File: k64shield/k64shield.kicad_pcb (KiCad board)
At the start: 2 copper layers, 7 parts, among them J1 top_left_header_02x08, J2 bottom_left_header_02x06, J3 rpi_motor_driver_header, J4 top_right_header_02x10, J5 bottom_right_header_02x08, J6 camera_header_01x05, J7 servo_header_01x03

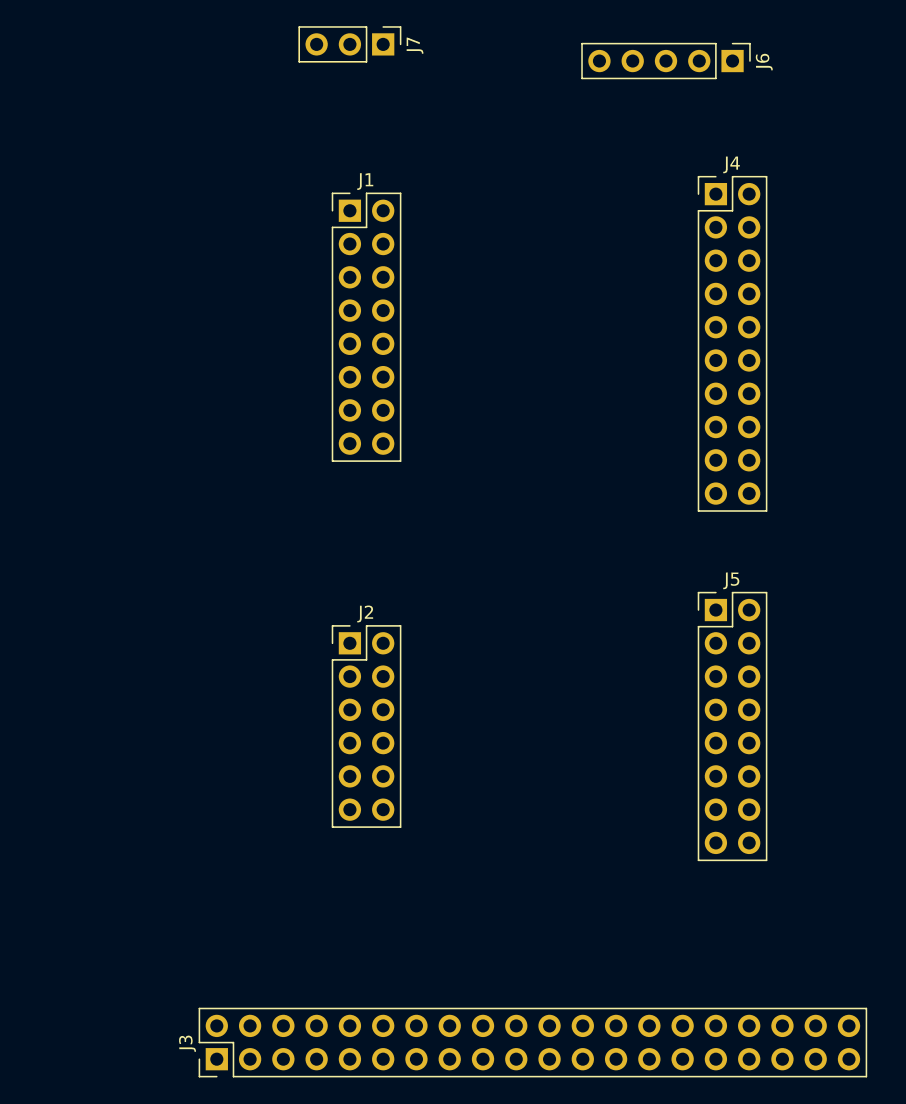
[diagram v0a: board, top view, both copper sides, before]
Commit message: Saving so I have a point to revert to - pins are very messed up
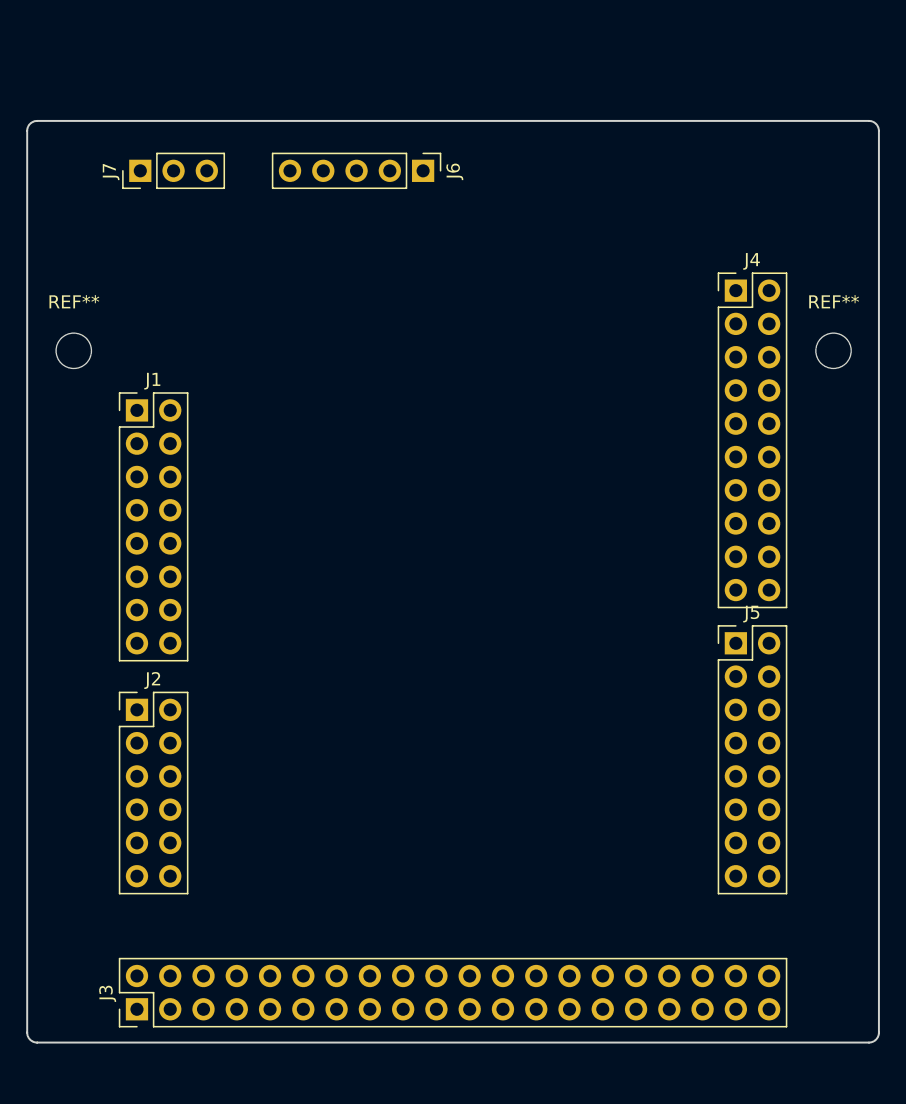
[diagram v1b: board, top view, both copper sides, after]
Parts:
- added REF**: MountingHole_2.7mm_M2.5, Mounting_Holes:MountingHole_2.7mm_M2.5, F.Cu at (149.9, 71.7)
- added REF**: MountingHole_2.7mm_M2.5, Mounting_Holes:MountingHole_2.7mm_M2.5, F.Cu at (91.9, 71.7)
- moved J6 25.1 mm to (118.6, 57.9)
- moved J1 22.3 mm to (96.8, 76.2)
- moved J7 20.9 mm to (97.0, 57.9), turned to 90 degrees
- moved J2 17.0 mm to (96.8, 99.1)
- moved J4 7.52 mm to (142.5, 67.1)
- moved J3 7.19 mm to (96.8, 121.9)
- moved J5 2.96 mm to (142.5, 94.0)
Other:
- board outline added: 65 x 70.4 mm
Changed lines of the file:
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@@
     (links 25)
     (no_connects 25)
-    (area 0 0 0 0)
+    (area 81.676572 49.378665 160.219429 129.802382)
     (thickness 1.6)
-    (drawings 0)
+    (drawings 8)
     (tracks 0)
     (zones 0)
-    (modules 7)
+    (modules 9)
     (nets 88)
   )
@@
     (pad_to_mask_clearance 0.2)
     (aux_axis_origin 0 0)
-    (visible_elements FFFFFF7F)
+    (grid_origin 79.248 130.556)
+    (visible_elements 7FFFFFFF)
     (pcbplotparams
       (layerselection 0x00030_80000001)
@@
     (add_net "Net-(J5-Pad9)")
   )
-  (module Pin_Headers:Pin_Header_Straight_2x08_Pitch2.54mm (layer F.Cu)
-    (at 113.03 60.96)
+  (module Mounting_Holes:MountingHole_2.7mm_M2.5 (layer F.Cu)
+    (at 149.948 71.65)
+    (descr "Mounting Hole 2.7mm, no annular, M2.5")
+    (tags "mounting hole 2.7mm no annular m2.5")
+    (attr virtual)
+    (fp_text reference REF** (at 0 -3.7) (layer F.SilkS)
+      (effects (font (size 1 1) (thickness 0.15)))
+    )
+    (fp_text value MountingHole_2.7mm_M2.5 (at 0 3.7) (layer F.Fab)
+      (effects (font (size 1 1) (thickness 0.15)))
+    )
+    (fp_text user %R (at 0.3 0) (layer F.Fab)
+      (effects (font (size 1 1) (thickness 0.15)))
+    )
+    (fp_circle (center 0 0) (end 2.7 0) (layer Cmts.User) (width 0.15))
+    (fp_circle (center 0 0) (end 2.95 0) (layer F.CrtYd) (width 0.05))
+    (pad 1 np_thru_hole circle (at 0 0) (size 2.7 2.7) (drill 2.7) (layers *.Cu *.Mask))
+  )
+  (module Pin_Headers:Pin_Header_Straight_2x08_Pitch2.54mm locked (layer F.Cu)
+    (at 96.774 76.2)
     (descr "Through hole straight pin header, 2x08, 2.54mm pitch, double rows")
     (tags "Through hole pin header THT 2x08 2.54mm double row")
@@
     )
   )
-  (module Pin_Headers:Pin_Header_Straight_2x06_Pitch2.54mm (layer F.Cu)
-    (at 113.03 93.98)
+  (module Pin_Headers:Pin_Header_Straight_2x06_Pitch2.54mm locked (layer F.Cu)
+    (at 96.774 99.06)
     (descr "Through hole straight pin header, 2x06, 2.54mm pitch, double rows")
     (tags "Through hole pin header THT 2x06 2.54mm double row")
@@
   )
   (module Pin_Headers:Pin_Header_Straight_2x20_Pitch2.54mm (layer F.Cu)
-    (at 102.87 125.73 90)
+    (at 96.774 121.92 90)
     (descr "Through hole straight pin header, 2x20, 2.54mm pitch, double rows")
     (tags "Through hole pin header THT 2x20 2.54mm double row")
@@
     )
   )
-  (module Pin_Headers:Pin_Header_Straight_2x10_Pitch2.54mm (layer F.Cu)
-    (at 140.97 59.69)
+  (module Pin_Headers:Pin_Header_Straight_2x10_Pitch2.54mm locked (layer F.Cu)
+    (at 142.494 67.056)
     (descr "Through hole straight pin header, 2x10, 2.54mm pitch, double rows")
     (tags "Through hole pin header THT 2x10 2.54mm double row")
@@
     )
   )
-  (module Pin_Headers:Pin_Header_Straight_2x08_Pitch2.54mm (layer F.Cu)
-    (at 140.97 91.44)
+  (module Pin_Headers:Pin_Header_Straight_2x08_Pitch2.54mm locked (layer F.Cu)
+    (at 142.494 93.98)
     (descr "Through hole straight pin header, 2x08, 2.54mm pitch, double rows")
     (tags "Through hole pin header THT 2x08 2.54mm double row")
@@
   )
   (module Pin_Headers:Pin_Header_Straight_1x05_Pitch2.54mm (layer F.Cu)
-    (at 142.24 49.53 270)
+    (at 118.618 57.912 270)
     (descr "Through hole straight pin header, 1x05, 2.54mm pitch, single row")
     (tags "Through hole pin header THT 1x05 2.54mm single row")
@@
   )
   (module Pin_Headers:Pin_Header_Straight_1x03_Pitch2.54mm (layer F.Cu)
-    (at 115.57 48.26 270)
+    (at 97.028 57.912 90)
     (descr "Through hole straight pin header, 1x03, 2.54mm pitch, single row")
     (tags "Through hole pin header THT 1x03 2.54mm single row")
-    (fp_text reference J7 (at 0 -2.33 270) (layer F.SilkS)
-      (effects (font (size 1 1) (thickness 0.15)))
-    )
-    (fp_text value servo_header_01x03 (at 0 7.41 270) (layer F.Fab)
+    (fp_text reference J7 (at 0 -2.33 90) (layer F.SilkS)
+      (effects (font (size 1 1) (thickness 0.15)))
+    )
+    (fp_text value servo_header_01x03 (at 0 7.41 90) (layer F.Fab)
       (effects (font (size 1 1) (thickness 0.15)))
     )
@@
     (fp_line (start 1.8 6.85) (end 1.8 -1.8) (layer F.CrtYd) (width 0.05))
     (fp_line (start 1.8 -1.8) (end -1.8 -1.8) (layer F.CrtYd) (width 0.05))
-    (fp_text user %R (at 0 2.54 360) (layer F.Fab)
-      (effects (font (size 1 1) (thickness 0.15)))
-    )
-    (pad 1 thru_hole rect (at 0 0 270) (size 1.7 1.7) (drill 1) (layers *.Cu *.Mask)
-      (net 12 /GND))
-    (pad 2 thru_hole oval (at 0 2.54 270) (size 1.7 1.7) (drill 1) (layers *.Cu *.Mask)
+    (fp_text user %R (at 0 2.54 180) (layer F.Fab)
+      (effects (font (size 1 1) (thickness 0.15)))
+    )
+    (pad 1 thru_hole rect (at 0 0 90) (size 1.7 1.7) (drill 1) (layers *.Cu *.Mask)
+      (net 12 /GND))
+    (pad 2 thru_hole oval (at 0 2.54 90) (size 1.7 1.7) (drill 1) (layers *.Cu *.Mask)
       (net 15 /5V))
-    (pad 3 thru_hole oval (at 0 5.08 270) (size 1.7 1.7) (drill 1) (layers *.Cu *.Mask)
+    (pad 3 thru_hole oval (at 0 5.08 90) (size 1.7 1.7) (drill 1) (layers *.Cu *.Mask)
       (net 80 /SIG))
     (model ${KISYS3DMOD}/Pin_Headers.3dshapes/Pin_Header_Straight_1x03_Pitch2.54mm.wrl
@@
     )
   )
+  (module Mounting_Holes:MountingHole_2.7mm_M2.5 (layer F.Cu)
+    (at 91.948 71.65)
+    (descr "Mounting Hole 2.7mm, no annular, M2.5")
+    (tags "mounting hole 2.7mm no annular m2.5")
+    (attr virtual)
+    (fp_text reference REF** (at 0 -3.7) (layer F.SilkS)
+      (effects (font (size 1 1) (thickness 0.15)))
+    )
+    (fp_text value MountingHole_2.7mm_M2.5 (at 0 3.7) (layer F.Fab)
+      (effects (font (size 1 1) (thickness 0.15)))
+    )
+    (fp_text user %R (at 0.3 0) (layer F.Fab)
+      (effects (font (size 1 1) (thickness 0.15)))
+    )
+    (fp_circle (center 0 0) (end 2.7 0) (layer Cmts.User) (width 0.15))
+    (fp_circle (center 0 0) (end 2.95 0) (layer F.CrtYd) (width 0.05))
+    (pad 1 np_thru_hole circle (at 0 0) (size 2.7 2.7) (drill 2.7) (layers *.Cu *.Mask))
+  )
+  (gr_line (start 88.392 54.864) (end 88.392 123.698) (angle 90) (layer Edge.Cuts) (width 0.15))
+  (gr_line (start 152.654 54.102) (end 89.154 54.102) (angle 90) (layer Edge.Cuts) (width 0.15))
+  (gr_line (start 153.416 123.698) (end 153.416 54.864) (angle 90) (layer Edge.Cuts) (width 0.15))
+  (gr_line (start 89.154 124.46) (end 152.654 124.46) (angle 90) (layer Edge.Cuts) (width 0.15))
+  (gr_arc (start 89.154 54.864) (end 88.392 54.864) (angle 90) (layer Edge.Cuts) (width 0.15))
+  (gr_arc (start 152.654 54.864) (end 152.654 54.102) (angle 90) (layer Edge.Cuts) (width 0.15))
+  (gr_arc (start 152.654 123.698) (end 153.416 123.698) (angle 90) (layer Edge.Cuts) (width 0.15))
+  (gr_arc (start 89.154 123.698) (end 89.154 124.46) (angle 90) (layer Edge.Cuts) (width 0.15))
 )

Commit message: Fixed all wiring. Everything is connected on PCB
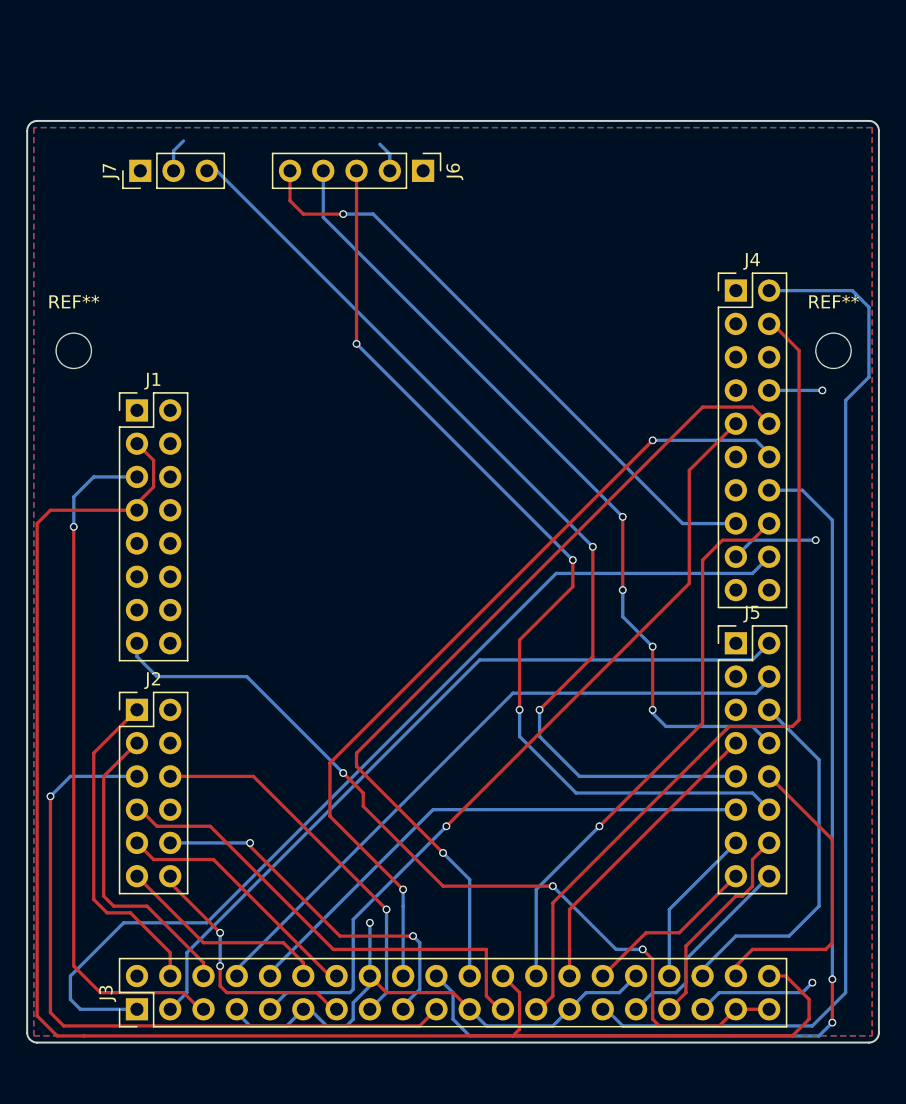
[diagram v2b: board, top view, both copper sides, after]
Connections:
- J1 pad 11: Net-(J1-Pad11) -> /GND
- J1 pad 12: /GND -> Net-(J1-Pad12)
- J1 pad 13: Net-(J1-Pad13) -> /GND
- J1 pad 14: /GND -> Net-(J1-Pad14)
- J1 pad 15: Net-(J1-Pad15) -> /5V
- J1 pad 16: /5V -> Net-(J1-Pad16)
- J1 pad 3: Net-(J1-Pad3) -> /3v3
- J1 pad 5: Net-(J1-Pad5) -> /RST
- J1 pad 7: Net-(J1-Pad7) -> /3v3
- J2 pad 1: Net-(J2-Pad1) -> /PTB2
- J2 pad 10: Net-(J2-Pad10) -> /PTB20
- J2 pad 11: Net-(J2-Pad11) -> /PTC10
- J2 pad 12: Net-(J2-Pad12) -> /DAC0_OUT
- J2 pad 3: Net-(J2-Pad3) -> /PTB3
- J2 pad 5: Net-(J2-Pad5) -> /PTB10
- J2 pad 6: Net-(J2-Pad6) -> /ADC1_DP1
- J2 pad 7: Net-(J2-Pad7) -> /PTB11
- J2 pad 9: Net-(J2-Pad9) -> /PTC11
- J3 pad 1: Net-(J3-Pad1) -> /B2
- J3 pad 10: Net-(J3-Pad10) -> /A1
- J3 pad 11: Net-(J3-Pad11) -> /GND
- J3 pad 12: Net-(J3-Pad12) -> /PTC10
- J3 pad 13: Net-(J3-Pad13) -> /DAC0_OUT
- J3 pad 14: /GND -> /PTC11
- J3 pad 15: Net-(J3-Pad15) -> /ADC1_DP1
- J3 pad 16: Net-(J3-Pad16) -> /GND
- J3 pad 17: Net-(J3-Pad17) -> /PTB20
- J3 pad 18: Net-(J3-Pad18) -> /PTD3
- J3 pad 19: Net-(J3-Pad19) -> /PTB10
- J3 pad 2: /5V -> /GND
- J3 pad 20: /GND -> /PTD2
- J3 pad 21: Net-(J3-Pad21) -> /GND
- J3 pad 22: Net-(J3-Pad22) -> /PTD1
- J3 pad 23: Net-(J3-Pad23) -> /PTB11
- J3 pad 24: Net-(J3-Pad24) -> /3v3
- J3 pad 25: /GND -> /PTE25
- J3 pad 26: Net-(J3-Pad26) -> /PTD0
- J3 pad 27: Net-(J3-Pad27) -> /GND
- J3 pad 28: Net-(J3-Pad28) -> /PTC9
- J3 pad 29: Net-(J3-Pad29) -> /PTE24
- J3 pad 3: Net-(J3-Pad3) -> /B1
- J3 pad 30: /GND -> /PTB18
- J3 pad 31: /A1 -> /Rx3
- J3 pad 32: Net-(J3-Pad32) -> /GND
- J3 pad 33: /A2 -> /Tx3
- J3 pad 34: /GND -> /PTB19
- J3 pad 35: Net-(J3-Pad35) -> /GND
- J3 pad 36: Net-(J3-Pad36) -> /PTA2
- J3 pad 37: Net-(J3-Pad37) -> /5V
- J3 pad 38: /B1 -> /PTA1
- J3 pad 39: /GND -> /5V
- J3 pad 4: /5V -> /PTB2
- J3 pad 40: /B2 -> /3v3
- J3 pad 5: Net-(J3-Pad5) -> /RST
- J3 pad 6: /GND -> /PTB3
- J3 pad 7: Net-(J3-Pad7) -> /GND
- J3 pad 8: Net-(J3-Pad8) -> /A2
- J3 pad 9: /GND -> /ADC1_DP0
- J4 pad 10: Net-(J4-Pad10) -> /PTD1
- J4 pad 12: Net-(J4-Pad12) -> /PTD3
- J4 pad 14: /GND -> /PTD2
- J4 pad 15: Net-(J4-Pad15) -> /AO
- J4 pad 16: Net-(J4-Pad16) -> /PTD0
- J4 pad 17: Net-(J4-Pad17) -> /GND
- J4 pad 18: Net-(J4-Pad18) -> /B2
- J4 pad 2: Net-(J4-Pad2) -> /PTE24
- J4 pad 3: /GND -> Net-(J4-Pad3)
- J4 pad 4: /B2 -> /PTE25
- J4 pad 5: /AO -> Net-(J4-Pad5)
- J4 pad 8: Net-(J4-Pad8) -> /GND
- J4 pad 9: Net-(J4-Pad9) -> /ADC1_DP0
- J5 pad 10: /SI -> /PTA1
- J5 pad 11: Net-(J5-Pad11) -> /A1
- J5 pad 12: Net-(J5-Pad12) -> /CLK
- J5 pad 13: Net-(J5-Pad13) -> /PTB19
- J5 pad 14: /A2 -> /Tx3
- J5 pad 15: Net-(J5-Pad15) -> /PTB18
- J5 pad 16: /B1 -> /Rx3
- J5 pad 2: Net-(J5-Pad2) -> /B1
- J5 pad 4: Net-(J5-Pad4) -> /A2
- J5 pad 5: /A1 -> Net-(J5-Pad5)
- J5 pad 6: /CLK -> /PTA2
- J5 pad 7: /SIG -> /PTC9
- J5 pad 8: Net-(J5-Pad8) -> /SI
- J5 pad 9: Net-(J5-Pad9) -> /SIG
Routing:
- net /3v3: track 0.00 -> 122.5 mm
- net /PTE24: track 0.00 -> 81.3 mm
- net /PTD2: track 0.00 -> 77.9 mm, vias 0 -> 2
- net /B2: track 0.00 -> 73.8 mm
- net /SIG: track 0.00 -> 73.8 mm, vias 0 -> 2
- net /CLK: track 0.00 -> 73.1 mm, vias 0 -> 3
- net /5V: track 0.00 -> 69.7 mm, vias 0 -> 3
- net /PTE25: track 0.00 -> 64.7 mm
- net /PTD1: track 0.00 -> 63.6 mm, vias 0 -> 1
- net /PTD3: track 0.00 -> 63.0 mm, vias 0 -> 2
- net /ADC1_DP0: track 0.00 -> 62.3 mm, vias 0 -> 1
- net /GND: track 0.00 -> 62.1 mm, vias 0 -> 4
- net /SI: track 0.00 -> 61.7 mm, vias 0 -> 4
- net /B1: track 0.00 -> 59.1 mm
- net /PTB10: track 0.00 -> 54.2 mm, vias 0 -> 1
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- added copper zone on B.Cu, net /5V
- added copper zone on F.Cu, net /GND

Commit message: Finished reroute
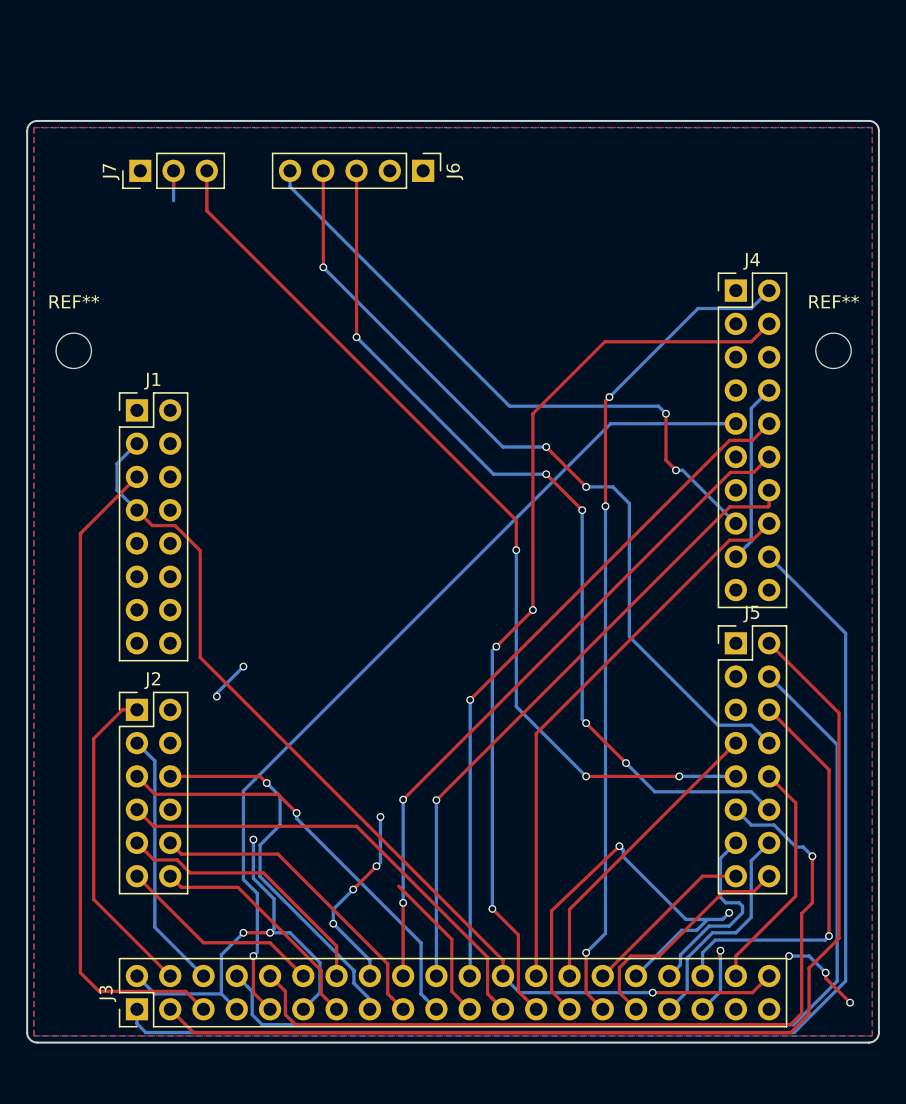
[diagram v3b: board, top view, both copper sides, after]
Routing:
- net /5V: track 69.7 -> 10.0 mm
- net /GND: track 62.1 -> 115.4 mm, vias 4 -> 12
- net /3v3: track 122.5 -> 75.9 mm, vias 0 -> 1
- net /PTD2: track 77.9 -> 49.3 mm, vias 2 -> 1
- net /A2: track 50.6 -> 75.2 mm
- net /B1: track 59.1 -> 81.6 mm
- net /A1: track 41.0 -> 63.2 mm, vias 0 -> 1
- net /PTB10: track 54.2 -> 32.8 mm
- net /B2: track 73.8 -> 91.9 mm
- net /PTE24: track 81.3 -> 63.6 mm, vias 0 -> 3
- net /PTD1: track 63.6 -> 52.7 mm
- net /PTD3: track 63.0 -> 52.2 mm
- net /PTA1: track 23.6 -> 18.0 mm
- net /ADC1_DP0: track 62.3 -> 67.0 mm
- net /CLK: track 73.1 -> 68.5 mm, vias 3 -> 5
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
